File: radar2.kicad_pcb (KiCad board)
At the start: 4 copper layers, 0 parts

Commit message: some changes to schematic nets, grouping passives and mosfets around our charger ic in pcb editor
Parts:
- added C1: 100pF, Capacitor_SMD:C_0603_1608Metric, F.Cu at (178.4, 152.8)
- added C10: 100pF, Capacitor_SMD:C_0603_1608Metric, F.Cu at (173.6, 151.8)
- added C11: 1uF, Capacitor_SMD:C_0603_1608Metric, F.Cu at (127.5, 144.1)
- added C12: 10uF, Capacitor_SMD:C_0603_1608Metric, F.Cu at (134.7, 139.4)
- added C13: 0.1uF, Capacitor_SMD:C_0603_1608Metric, F.Cu at (140.7, 139.3)
- added C14: 0.1uF, Capacitor_SMD:C_0603_1608Metric, F.Cu at (144.8, 139.2)
- added C15: 0.1uF, Capacitor_SMD:C_0603_1608Metric, F.Cu at (142.7, 139.2)
- added C16: 0.1uF, Capacitor_SMD:C_0603_1608Metric, F.Cu at (138.8, 139.3)
- added C17: 0.1uF, Capacitor_SMD:C_0603_1608Metric, F.Cu at (136.8, 139.3)
- added C18: 470nF, Capacitor_SMD:C_0603_1608Metric, F.Cu at (150.9, 139.2)
- added C19: 33nF, Capacitor_SMD:C_0603_1608Metric, F.Cu at (156.8, 147.2)
- added C2: 680pF, Capacitor_SMD:C_0603_1608Metric, F.Cu at (191.1, 145.7)
- added C20: 33nF, Capacitor_SMD:C_0603_1608Metric, F.Cu at (160.7, 146.1)
- added C21: 10nF, Capacitor_SMD:C_0603_1608Metric, F.Cu at (165.4, 141.2)
- added C22: 47nF, Capacitor_SMD:C_0603_1608Metric, F.Cu at (176.1, 130.4)
- added C23: 47nF, Capacitor_SMD:C_0603_1608Metric, F.Cu at (184.1, 130.2)
- added C24: 0.1uF, Capacitor_SMD:C_0603_1608Metric, F.Cu at (209.2, 138.8)
- added C25: 0.1uF, Capacitor_SMD:C_0603_1608Metric, F.Cu at (206.7, 138.8)
- added C26: 0.1uF, Capacitor_SMD:C_0603_1608Metric, F.Cu at (204.2, 138.8)
- added C27: 0.1uF, Capacitor_SMD:C_0603_1608Metric, F.Cu at (201.7, 138.8)
- added C28: 0.1uF, Capacitor_SMD:C_0603_1608Metric, F.Cu at (199.2, 138.8)
- added C29: 10uF, Capacitor_SMD:C_0603_1608Metric, F.Cu at (196.7, 138.8)
- added C3: 33pF, Capacitor_SMD:C_0603_1608Metric, F.Cu at (183.3, 144.1)
- added C30: 1uF, Capacitor_SMD:C_0603_1608Metric, F.Cu at (201.1, 149.0)
- added C31: 0.1uF, Capacitor_SMD:C_0603_1608Metric, F.Cu at (206.0, 148.9)
- added C32: 4.7uF, Capacitor_SMD:C_0603_1608Metric, F.Cu at (152.7, 60.4)
- added C33: 4.7uF, Capacitor_SMD:C_0603_1608Metric, F.Cu at (156.7, 37.8)
- added C34: 4.7uF, Capacitor_SMD:C_0603_1608Metric, F.Cu at (156.7, 40.3)
- added C35: 4.7uF, Capacitor_SMD:C_0603_1608Metric, F.Cu at (156.7, 42.8)
- added C36: 0.1uF, Capacitor_SMD:C_0603_1608Metric, F.Cu at (156.7, 45.4)
- added C37: 100uF, Capacitor_SMD:C_0603_1608Metric, F.Cu at (156.7, 47.9)
- added C38: 100uF, Capacitor_SMD:C_0603_1608Metric, F.Cu at (156.7, 50.4)
- added C39: 4700pf, Capacitor_SMD:C_0603_1608Metric, F.Cu at (156.7, 52.9)
- added C4: 33pF, Capacitor_SMD:C_0603_1608Metric, F.Cu at (188.7, 154.2)
- added C40: 47pf, Capacitor_SMD:C_0603_1608Metric, F.Cu at (156.7, 55.4)
- added C41: 4.7uF, Capacitor_SMD:C_0603_1608Metric, F.Cu at (156.7, 57.9)
- added C42: 4.7uF, Capacitor_SMD:C_0603_1608Metric, F.Cu at (156.7, 60.4)
- added C43: 4.7uF, Capacitor_SMD:C_0603_1608Metric, F.Cu at (160.7, 37.8)
- added C44: 4.7uF, Capacitor_SMD:C_0603_1608Metric, F.Cu at (160.7, 40.3)
- added C45: 0.1uF, Capacitor_SMD:C_0603_1608Metric, F.Cu at (160.7, 42.8)
- added C46: 4700pf, Capacitor_SMD:C_0603_1608Metric, F.Cu at (160.7, 45.4)
- added C47: 100uF, Capacitor_SMD:C_0603_1608Metric, F.Cu at (160.7, 47.9)
- added C48: 47pf, Capacitor_SMD:C_0603_1608Metric, F.Cu at (160.7, 50.4)
- added C49: 100uF, Capacitor_SMD:C_0603_1608Metric, F.Cu at (160.7, 52.9)
- added C5: 1800pF, Capacitor_SMD:C_0603_1608Metric, F.Cu at (183.0, 154.4)
- added C50: 0.1uF, Capacitor_SMD:C_0603_1608Metric, F.Cu at (65.9, 117.7)
- added C51: 0.22uF, Capacitor_SMD:C_0603_1608Metric, F.Cu at (76.8, 122.5)
- added C52: 47uF, Capacitor_SMD:C_0603_1608Metric, F.Cu at (72.2, 119.5)
- added C53: 1uF, Capacitor_SMD:C_0603_1608Metric, F.Cu at (68.1, 124.0)
- added C54: 3.3pF, Capacitor_SMD:C_0603_1608Metric, F.Cu at (74.9, 130.1)
- added C55: 3.3pF, Capacitor_SMD:C_0603_1608Metric, F.Cu at (68.7, 129.9)
- added C56: 47uF, Capacitor_SMD:C_0603_1608Metric, F.Cu at (76.8, 124.5)
- added C57: 47uF, Capacitor_SMD:C_0603_1608Metric, F.Cu at (68.2, 121.9)
- added C58: 47uF, Capacitor_SMD:C_0603_1608Metric, F.Cu at (76.8, 120.8)
- added C59: 0.1uF, Capacitor_SMD:C_0603_1608Metric, F.Cu at (173.0, 73.6)
- added C6: 0.1muF, Capacitor_SMD:C_0603_1608Metric, F.Cu at (127.4, 138.1)
- added C60: 0.1uF, Capacitor_SMD:C_0603_1608Metric, F.Cu at (173.0, 76.1)
- added C61: 0.1uF, Capacitor_SMD:C_0603_1608Metric, F.Cu at (173.0, 78.7)
- added C62: 0.1uF, Capacitor_SMD:C_0603_1608Metric, F.Cu at (173.0, 81.2)
- added C63: 0.1uF, Capacitor_SMD:C_0603_1608Metric, F.Cu at (173.0, 83.7)
- added C64: 0.1uF, Capacitor_SMD:C_0603_1608Metric, F.Cu at (173.0, 86.2)
- added C65: 0.1uF, Capacitor_SMD:C_0603_1608Metric, F.Cu at (177.0, 73.6)
- added C66: 0.1uF, Capacitor_SMD:C_0603_1608Metric, F.Cu at (177.0, 76.1)
- added C67: 0.1uF, Capacitor_SMD:C_0603_1608Metric, F.Cu at (177.0, 78.7)
- added C68: 0.1uF, Capacitor_SMD:C_0603_1608Metric, F.Cu at (177.0, 81.2)
- added C69: 0.1uF, Capacitor_SMD:C_0603_1608Metric, F.Cu at (177.0, 83.7)
- added C7: 22muF, Capacitor_SMD:C_0603_1608Metric, F.Cu at (120.4, 142.7)
- added C70: 4.7uF, Capacitor_SMD:C_0603_1608Metric, F.Cu at (177.0, 86.2)
- added C71: 0.1uF, Capacitor_SMD:C_0603_1608Metric, F.Cu at (181.0, 73.6)
- added C72: 4.7uF, Capacitor_SMD:C_0603_1608Metric, F.Cu at (181.0, 76.1)
- added C73: 0.1uF, Capacitor_SMD:C_0603_1608Metric, F.Cu at (92.2, 94.0)
- added C74: 4.7uF, Capacitor_SMD:C_0603_1608Metric, F.Cu at (181.0, 78.7)
- added C75: 0.1uF, Capacitor_SMD:C_0603_1608Metric, F.Cu at (69.4, 86.4)
- added C76: 0.1uF, Capacitor_SMD:C_0603_1608Metric, F.Cu at (79.5, 73.7)
- added C8: 1uF, Capacitor_SMD:C_0603_1608Metric, F.Cu at (168.6, 146.2)
- added C9: 3.3uF, Capacitor_SMD:C_0603_1608Metric, F.Cu at (180.1, 140.8)
- added D1: PDS760-13, sbr8u:POWERDI5, F.Cu at (95.6, 61.7)
- added D2: PDS760-13, sbr8u:POWERDI5, F.Cu at (101.6, 45.7)
- added IC1: BQ25713RSNR, bq2517:QFN40P400X400X80-33N-D, F.Cu at (179.0, 146.0)
- added IC2: TPS54540DDA, tps54:SOIC127P600X170-9N, F.Cu at (179.0, 39.8)
- added IC3: TPS54540DDA, tps54:SOIC127P600X170-9N, F.Cu at (179.0, 46.4)
- added IC4: DW3120TR13, dw3120:DW3120TR13, F.Cu at (72.5, 123.1)
- added J1: GSB1C4621DS1HR, gsb_usb:GSB, F.Cu at (114.0, 151.0)
- added J2: M20-8770546 (for SWD), Connector_PinSocket_2.54mm:PinSocket_1x05_P2.54mm_Vertical, F.Cu at (58.4, 76.2)
- added J3: M20-8770342 (for RasPi), Connector_PinSocket_2.54mm:PinSocket_1x03_P2.54mm_Vertical, F.Cu at (58.4, 99.1)
- added J4: JST-XH, Connector_JST:JST_XH_B2B-XH-AM_1x02_P2.50mm_Vertical, F.Cu at (220.5, 146.1)
- added J6: SMA_CONNECTOR, sma_conn1:SMACONNECTOR, F.Cu at (99.1, 129.5)
- added J7: SMA_CONNECTOR, sma_conn1:SMACONNECTOR, F.Cu at (88.9, 129.5)
- added L1: 2.2uH, Inductor_SMD:L_0603_1608Metric, F.Cu at (179.9, 127.2)
- added L2: 5.5uH, Inductor_SMD:L_0603_1608Metric, F.Cu at (160.7, 57.9)
- added L3: 5.5uH, Inductor_SMD:L_0603_1608Metric, F.Cu at (160.7, 60.4)
- added Q1: CSD17308Q3, csd17:CSD17308Q3, F.Cu at (170.6, 137.5)
- added Q2: CSD17308Q3, csd17:CSD17308Q3, F.Cu at (170.9, 130.4)
- added Q3: CSD17308Q3, csd17:CSD17308Q3, F.Cu at (190.0, 130.5)
- added Q4: CSD17308Q3, csd17:CSD17308Q3, F.Cu at (189.9, 137.5)
- added Q5: CSD25404Q3, csd25:DQG_VSON-CLIP, F.Cu at (196.6, 146.8)
- added R1: 30k, Resistor_SMD:R_0603_1608Metric, F.Cu at (180.4, 151.5)
- added R10: 220k, Resistor_SMD:R_0603_1608Metric, F.Cu at (172.8, 148.9)
- added R11: 220k, Resistor_SMD:R_0603_1608Metric, F.Cu at (168.7, 150.9)
- added R12: 2.2, Resistor_SMD:R_0603_1608Metric, F.Cu at (127.5, 141.3)
- added R13: 4.99, Resistor_SMD:R_0603_1608Metric, F.Cu at (155.0, 143.4)
- added R14: 4.99, Resistor_SMD:R_0603_1608Metric, F.Cu at (161.7, 143.3)
- added R15: 1, Resistor_SMD:R_0603_1608Metric, F.Cu at (150.9, 134.9)
- added R16: 10m, Resistor_SMD:R_0603_1608Metric, F.Cu at (206.0, 144.6)
- added R17: 10, Resistor_SMD:R_0603_1608Metric, F.Cu at (204.1, 154.2)
- added R18: 10, Resistor_SMD:R_0603_1608Metric, F.Cu at (208.8, 154.4)
- added R19: 243k, Resistor_SMD:R_0603_1608Metric, F.Cu at (168.7, 52.9)
- added R2: 10k, Resistor_SMD:R_0603_1608Metric, F.Cu at (187.3, 144.9)
- added R20: 365k, Resistor_SMD:R_0603_1608Metric, F.Cu at (168.7, 55.4)
- added R21: 88.7k, Resistor_SMD:R_0603_1608Metric, F.Cu at (168.7, 57.9)
- added R22: 16.9k, Resistor_SMD:R_0603_1608Metric, F.Cu at (168.7, 60.4)
- added R23: 31.6k, Resistor_SMD:R_0603_1608Metric, F.Cu at (172.7, 37.8)
- added R24: 10.2k, Resistor_SMD:R_0603_1608Metric, F.Cu at (172.7, 40.3)
- added R25: 365k, Resistor_SMD:R_0603_1608Metric, F.Cu at (172.7, 42.8)
- added R26: 88.7k, Resistor_SMD:R_0603_1608Metric, F.Cu at (172.7, 45.4)
- added R27: 243k, Resistor_SMD:R_0603_1608Metric, F.Cu at (172.7, 47.9)
- added R28: 16.9k, Resistor_SMD:R_0603_1608Metric, F.Cu at (172.7, 50.4)
- added R29: 31.6k, Resistor_SMD:R_0603_1608Metric, F.Cu at (172.7, 52.9)
- added R3: 40.2k, Resistor_SMD:R_0603_1608Metric, F.Cu at (186.3, 151.4)
- added R30: 10.2k, Resistor_SMD:R_0603_1608Metric, F.Cu at (172.7, 55.4)
- added R31: 100k, Resistor_SMD:R_0603_1608Metric, F.Cu at (75.4, 83.8)
- added R32: 10k, Resistor_SMD:R_0603_1608Metric, F.Cu at (75.4, 86.4)
- added R33: 10k, Resistor_SMD:R_0603_1608Metric, F.Cu at (81.3, 83.8)
- added R34: 10k, Resistor_SMD:R_0603_1608Metric, F.Cu at (81.3, 86.4)
- added R35: 10k, Resistor_SMD:R_0603_1608Metric, F.Cu at (81.3, 78.7)
- added R36: 10k, Resistor_SMD:R_0603_1608Metric, F.Cu at (88.9, 88.9)
- added R37: 10m, Resistor_SMD:R_0603_1608Metric, F.Cu at (157.6, 139.3)
- added R38: 10k, Resistor_SMD:R_0603_1608Metric, F.Cu at (86.4, 86.4)
- added R4: 250k, Resistor_SMD:R_0603_1608Metric, F.Cu at (184.8, 148.3)
- added R5: 350k, Resistor_SMD:R_0603_1608Metric, F.Cu at (176.5, 150.2)
- added R6: 10, Resistor_SMD:R_0603_1608Metric, F.Cu at (174.4, 141.4)
- added R7: 5k, Resistor_SMD:R_0603_1608Metric, F.Cu at (109.0, 143.0)
- added R8: 5k, Resistor_SMD:R_0603_1608Metric, F.Cu at (115.5, 143.6)
- added R9: 383k, Resistor_SMD:R_0603_1608Metric, F.Cu at (172.8, 144.0)
- added SW1: 09.03290.01, 09111:090329001, F.Cu at (86.4, 73.7)
- added SW2: SWT0220-016016GSA, button:SWT0220016016GSA, F.Cu at (71.1, 73.7)
- added U1: STM32H725ZETx, Package_QFP:LQFP-144_20x20mm_P0.5mm, B.Cu at (76.2, 101.6)
- added Y1: ECS-384-CDX-2482, Crystal:Crystal_SMD_2016-4Pin_2.0x1.6mm, F.Cu at (71.8, 130.1)

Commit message: working on LDOs
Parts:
- moved D2 144.0 mm to (245.1, 58.5), turned to 90 degrees
- moved C49 91.5 mm to (252.1, 50.2), turned to 90 degrees
- moved L3 91.5 mm to (251.9, 54.0), turned to 90 degrees
- moved C46 89.5 mm to (248.4, 63.2), turned to -90 degrees
- moved C47 87.3 mm to (247.8, 52.5)
- moved C48 85.7 mm to (245.5, 63.0), turned to -90 degrees
- moved R29 82.0 mm to (253.6, 66.3), turned to -90 degrees
- moved R30 79.3 mm to (251.3, 66.2), turned to 90 degrees
- moved C45 77.9 mm to (237.1, 57.8), turned to 180 degrees
- moved C41 77.7 mm to (234.2, 62.5), turned to -90 degrees
- moved R28 75.6 mm to (246.8, 65.6)
- moved C42 75.0 mm to (231.7, 62.5), turned to -90 degrees
- moved C43 73.2 mm to (229.6, 62.5), turned to -90 degrees
- moved C44 70.0 mm to (227.1, 62.5), turned to -90 degrees
- moved R27 64.8 mm to (233.6, 69.9), turned to 180 degrees
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
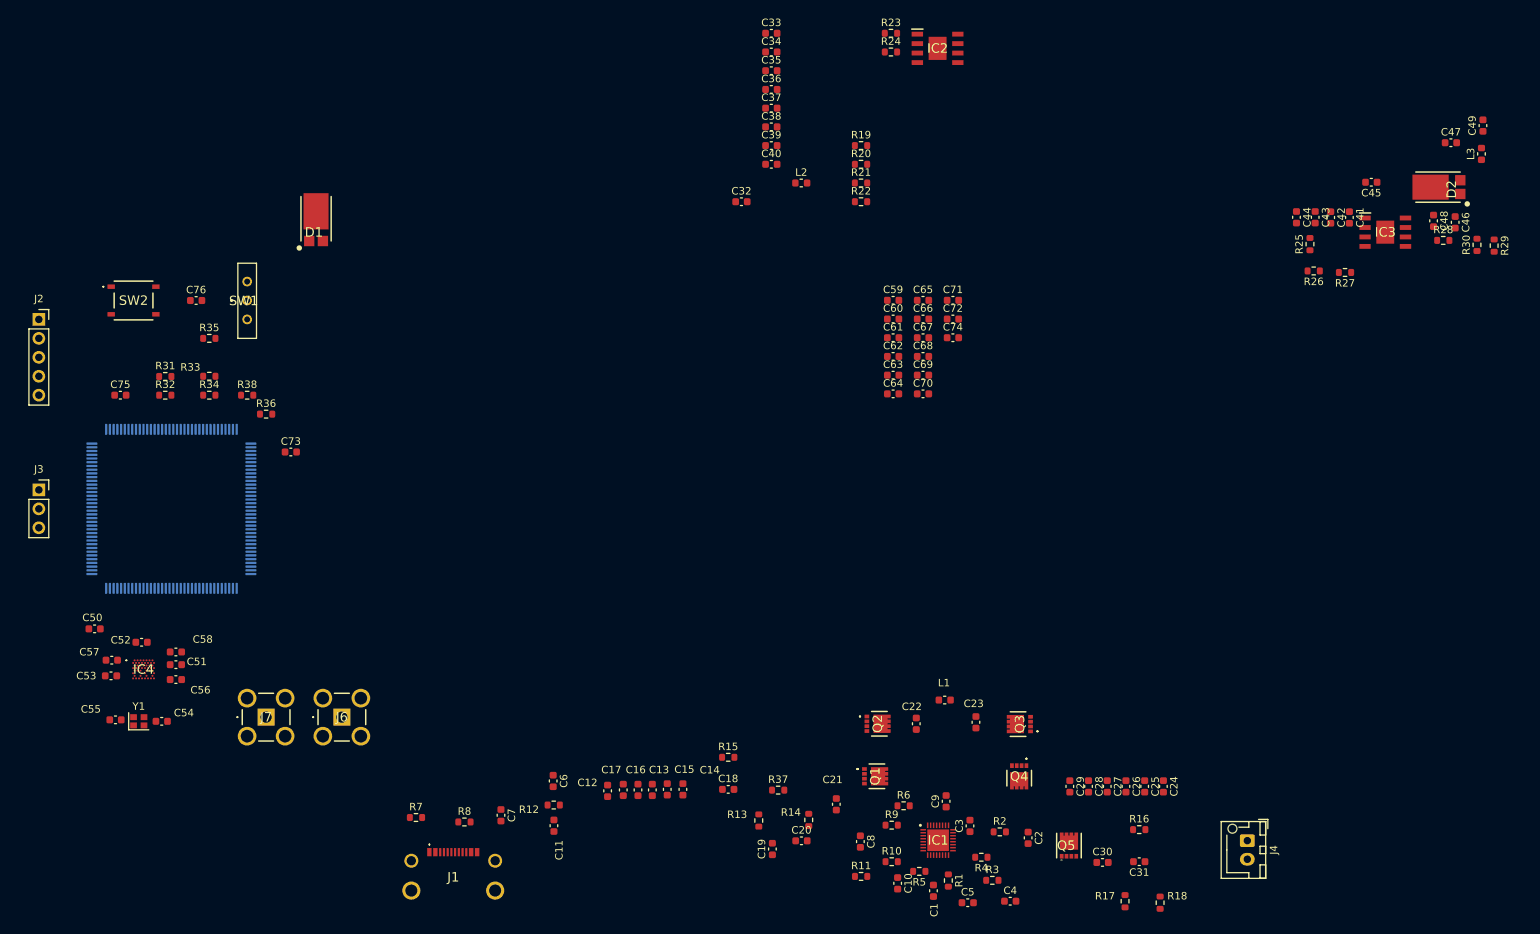
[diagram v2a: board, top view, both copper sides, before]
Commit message: fixing silk screens for passives
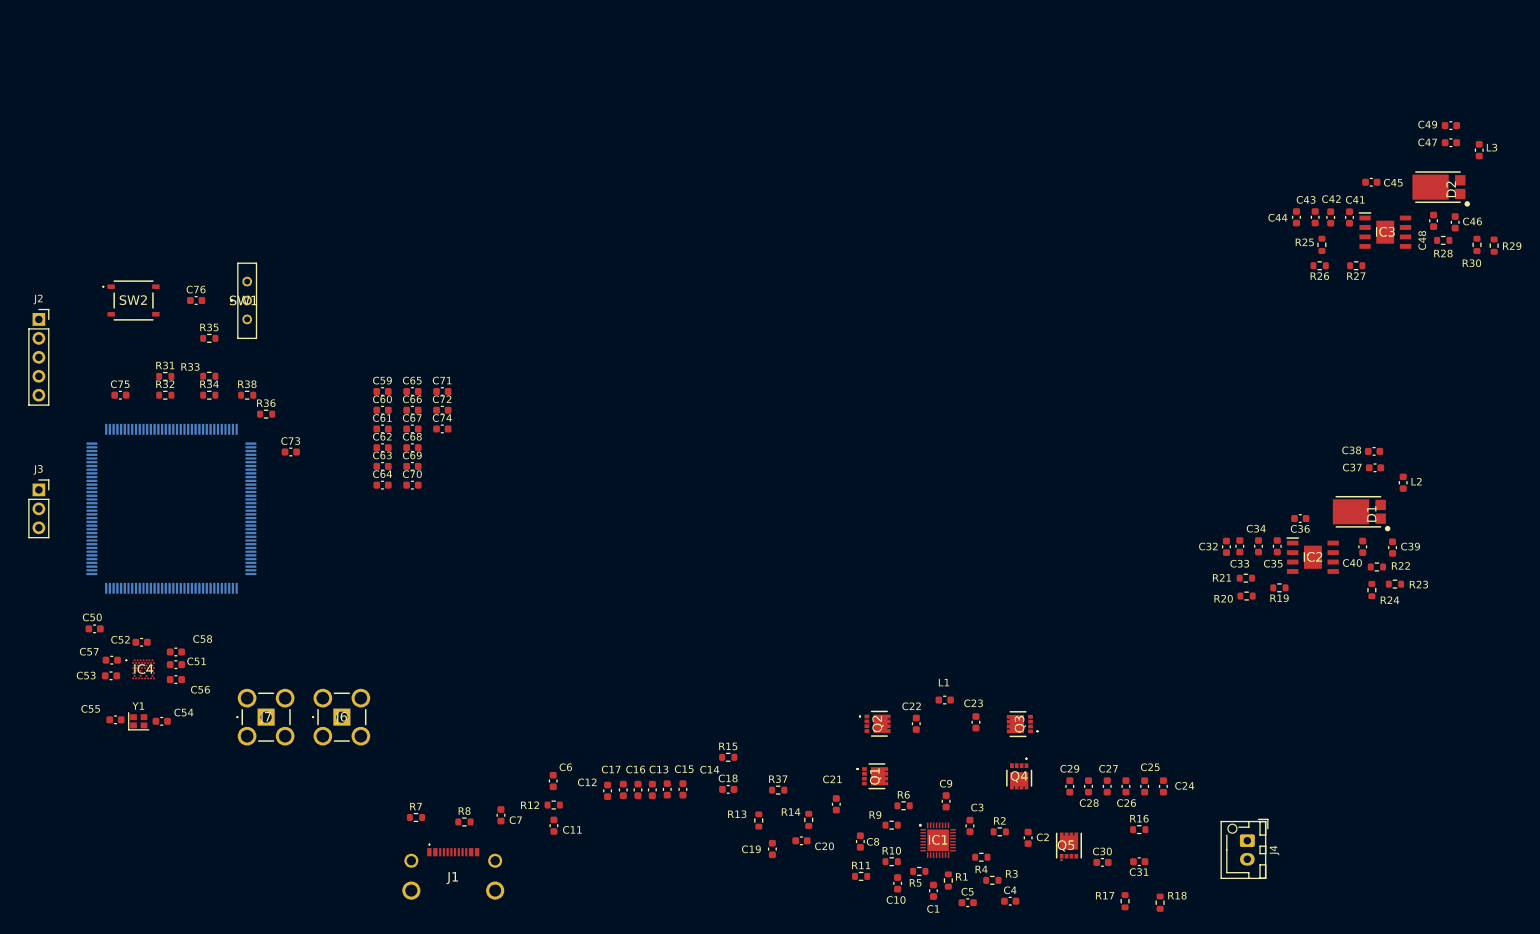
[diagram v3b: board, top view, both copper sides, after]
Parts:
- moved D1 144.5 mm to (234.4, 102.0), turned to 90 degrees
- moved R23 100.1 mm to (240.3, 111.7), turned to 180 degrees
- moved C39 99.2 mm to (240.0, 106.8), turned to -90 degrees
- moved R24 96.8 mm to (237.2, 112.5), turned to -90 degrees
- moved C40 94.5 mm to (236.0, 106.7), turned to -90 degrees
- moved C37 94.2 mm to (237.6, 96.1)
- moved C33 93.2 mm to (219.5, 106.6), turned to 90 degrees
- moved C35 93.1 mm to (224.5, 106.6), turned to 90 degrees
- moved C34 93.1 mm to (222.0, 106.6), turned to 90 degrees
- moved C38 91.8 mm to (237.5, 93.9)
- moved C36 91.3 mm to (227.6, 102.9), turned to 180 degrees
- moved L2 90.2 mm to (241.4, 98.1), turned to 90 degrees
- moved IC2 84.8 mm to (229.3, 108.1)
- moved R22 84.8 mm to (237.9, 109.4)
- moved R19 81.7 mm to (224.8, 112.2), turned to 180 degrees
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
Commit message: adding connectors for display and pi power, pin headers
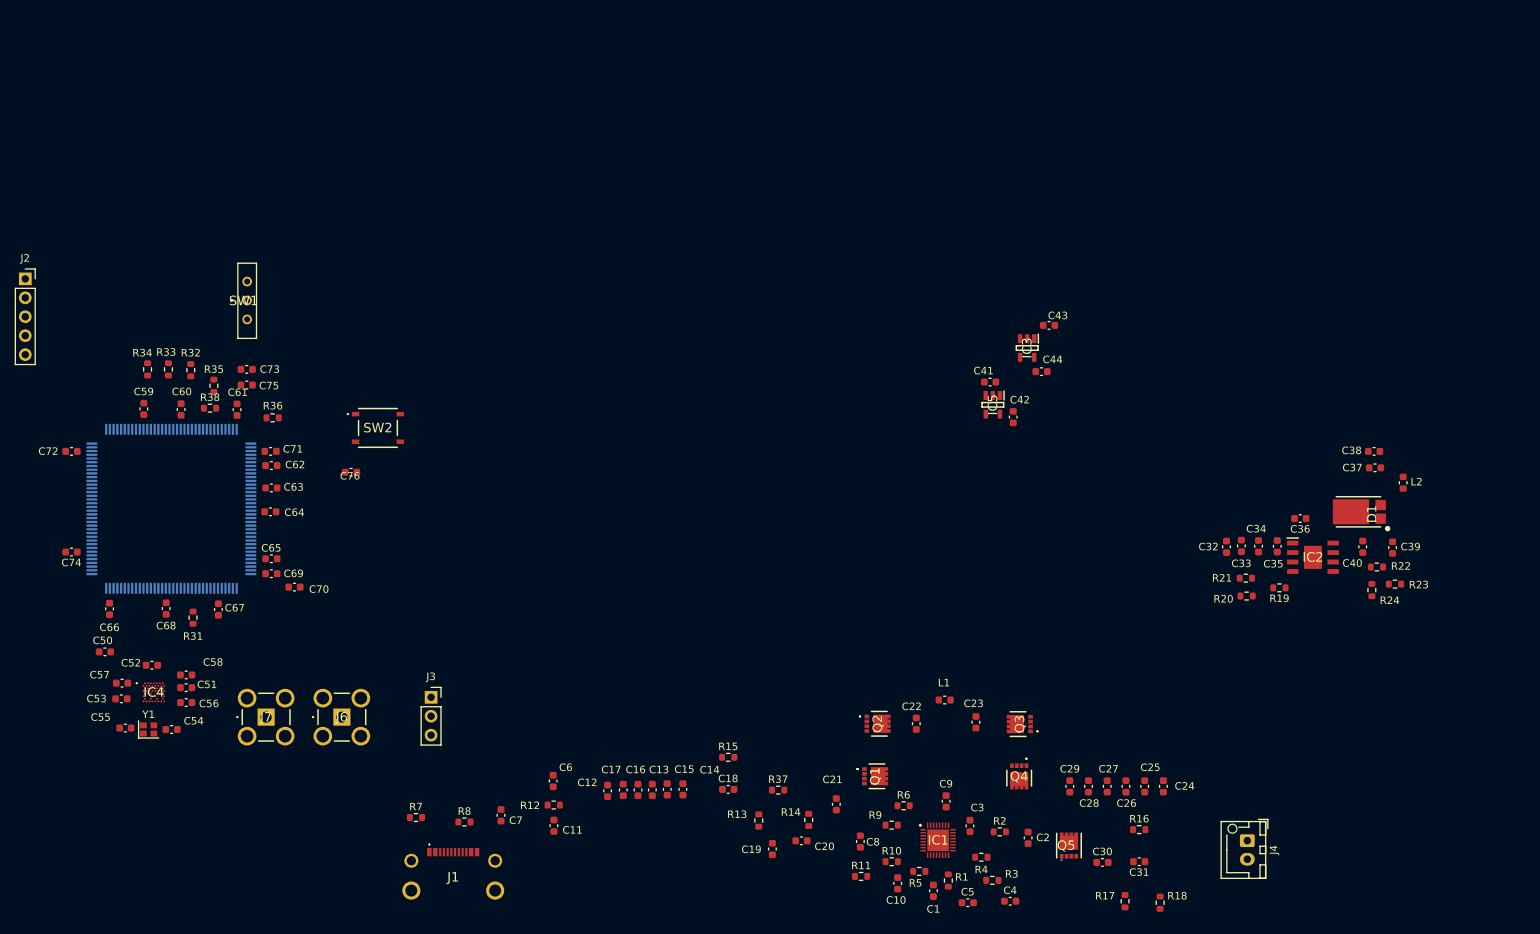
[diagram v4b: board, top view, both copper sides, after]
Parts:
- removed C45: 0.1uF, Capacitor_SMD:C_0603_1608Metric
- removed C46: 4700pf, Capacitor_SMD:C_0603_1608Metric
- removed C47, C49: 100uF, Capacitor_SMD:C_0603_1608Metric
- removed C48: 47pf, Capacitor_SMD:C_0603_1608Metric
- removed D2: PDS760-13, sbr8u:POWERDI5
- removed L3: 5.5uH, Inductor_SMD:L_0603_1608Metric
- removed R25: 365k, Resistor_SMD:R_0603_1608Metric
- removed R26: 88.7k, Resistor_SMD:R_0603_1608Metric
- removed R27: 243k, Resistor_SMD:R_0603_1608Metric
- removed R28: 16.9k, Resistor_SMD:R_0603_1608Metric
- removed R29: 31.6k, Resistor_SMD:R_0603_1608Metric
- removed R30: 10.2k, Resistor_SMD:R_0603_1608Metric
- added IC5: LP5907QMFX-3.0Q1, lp59:SOT95P280X145-5N, F.Cu at (186.4, 87.7)
- C41, C42, C43, C44: value 4.7uF -> 1uF
- IC3: value TPS54540DDA -> LP5907QMFX-3.0Q1; footprint tps54:SOIC127P600X170-9N -> lp59:SOT95P280X145-5N
- moved J3 59.5 mm to (111.0, 126.9)
- moved C41 53.0 mm to (186.0, 84.6), turned to 180 degrees
- moved C74 52.4 mm to (62.8, 107.4), turned to 180 degrees
- moved IC3 50.5 mm to (191.0, 80.0), turned to -90 degrees
- moved C42 50.3 mm to (189.1, 89.3), turned to 90 degrees
- moved C72 50.0 mm to (62.8, 93.9)
- moved C66 48.6 mm to (67.9, 115.0), turned to -90 degrees
- moved C44 40.0 mm to (192.9, 83.2), turned to 180 degrees
- moved C68 39.4 mm to (75.5, 115.0), turned to 90 degrees
- moved C43 38.5 mm to (193.9, 77.0), turned to 180 degrees
- moved SW2 37.0 mm to (103.9, 90.8)
- moved C67 35.5 mm to (82.5, 115.1), turned to -90 degrees
- moved R31 32.6 mm to (79.1, 116.2), turned to 90 degrees
- moved C59 32.1 mm to (72.5, 88.2), turned to 90 degrees
- moved C76 31.0 mm to (100.3, 96.7), turned to 180 degrees
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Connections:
- C37 pad 2: DW_VDD1 -> VOUT
- C38 pad 2: DW_VDD1 -> VOUT
- C41 pad 2: Net-(IC3-VIN) -> VOUT
- C42 pad 2: Net-(IC3-VIN) -> 3V3_MCU
- C43 pad 2: Net-(IC3-VIN) -> VOUT
- C44 pad 2: Net-(IC3-VIN) -> 3V3_RADAR
- C52 pad 1: DW_VDD1 -> 3V3_RADAR
- C53 pad 1: DW_VDD1 -> 3V3_RADAR
- C56 pad 1: DW_VDD1 -> 3V3_RADAR
- C57 pad 1: DW_VDD1 -> 3V3_RADAR
- C58 pad 1: DW_VDD1 -> 3V3_RADAR
- C59 pad 1: VDD -> 3V3_MCU
- C60 pad 1: VDD -> 3V3_MCU
- C61 pad 1: VDD -> 3V3_MCU
- C62 pad 1: VDD -> 3V3_MCU
- C63 pad 1: VDD -> 3V3_MCU
- C64 pad 1: VDD -> 3V3_MCU
- C65 pad 1: VDD -> 3V3_MCU
- C66 pad 1: VDD -> 3V3_MCU
- C67 pad 1: VDD -> 3V3_MCU
- C68 pad 1: VDD -> 3V3_MCU
- C69 pad 1: VDD -> 3V3_MCU
- C70 pad 1: VDD -> 3V3_MCU
- C71 pad 1: VDD -> 3V3_MCU
- C72 pad 1: VDD -> 3V3_MCU
- C74 pad 1: VDD -> 3V3_MCU
- IC3 pad 1: Net-(IC3-BOOT) -> VOUT
- IC3 pad 2: Net-(IC3-VIN) -> GND
- IC3 pad 3: Net-(IC3-EN) -> VOUT
- IC3 pad 4: Net-(IC3-RT/CLK) -> unconnected-(IC3-N/C-Pad4)
- IC3 pad 5: /pmics/FB2 -> 3V3_MCU
- IC4 pad B13: DW_VDD1 -> 3V3_RADAR
- IC4 pad B15: DW_VDD1 -> 3V3_RADAR
- IC4 pad D15: DW_VDD1 -> 3V3_RADAR
- IC4 pad F15: DW_VDD1 -> 3V3_RADAR
- J2 pad 1: VDD -> 3V3_MCU
- L2 pad 2: DW_VDD1 -> VOUT
- Q4 pad 5: /pmics/VSYS -> GND
- Q4 pad 6: /pmics/VSYS -> GND
- Q4 pad 7: /pmics/VSYS -> GND
- Q4 pad 8: /pmics/VSYS -> GND
- Q4 pad 9: /pmics/VSYS -> GND
- Q5 pad 5: /pmics/VSYS -> GND
- Q5 pad 6: /pmics/VSYS -> GND
- Q5 pad 7: /pmics/VSYS -> GND
- Q5 pad 8: /pmics/VSYS -> GND
- R23 pad 1: DW_VDD1 -> VOUT
- R32 pad 1: VDD -> 3V3_MCU
- R33 pad 2: VDD -> 3V3_MCU
- R34 pad 1: VDD -> 3V3_MCU
- R36 pad 2: VDD -> 3V3_MCU
- R38 pad 1: VDD -> 3V3_MCU
- SW1 pad 3: VDD -> 3V3_MCU
- U1 pad 106: VDD -> 3V3_MCU
- U1 pad 119: VDD -> 3V3_MCU
- U1 pad 129: VDD -> 3V3_MCU
- U1 pad 13: VDD -> 3V3_MCU
- U1 pad 144: VDD -> 3V3_MCU
- U1 pad 19: VDD -> 3V3_MCU
- U1 pad 32: VDD -> 3V3_MCU
- U1 pad 35: VDD -> 3V3_MCU
- U1 pad 36: VDD -> 3V3_MCU
- U1 pad 42: VDD -> 3V3_MCU
- U1 pad 56: VDD -> 3V3_MCU
- U1 pad 7: VDD -> 3V3_MCU
- U1 pad 71: VDD -> 3V3_MCU
- U1 pad 79: VDD -> 3V3_MCU
- U1 pad 90: VDD -> 3V3_MCU
- U1 pad 91: VDD -> 3V3_MCU
- U1 pad 92: VDD -> 3V3_MCU
